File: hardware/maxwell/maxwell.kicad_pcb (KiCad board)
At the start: 2 copper layers, 122 x 59 mm, 91 parts, among them J1 Canbus 1, J10 SPI2_B, J11 BACKUP, J12 UART4, J13 UART5, J14 I2C1, J16 ESP_BM, J17 ESP_PROG, J19 Interconnect (Power), J2 SPI2_C, J20 Interconnect (uC), J3 Neopixel, J4 BOOT0, J5 SPI2_A, J6 Programmer, J7 Dynamo Input, J8 BOOT1, J9 Battery, Q1 BSS138, Q2 PSMN5R4-25YLD, Q3 DMN2400UV, Q4 NTR1P02T1, Q5 NTR1P02T1, U1 MCP1501, U10 MIC39102, U11 AP9101C, U2 SN65HVD233, U3 TPS2113, U4 PCA9536D, U5 ESP-32S, U6 AD7991, U7 STM32F103RETx, U8 TLP188, U9 Buck Regulator, Y1 32.768k, Y2 8M

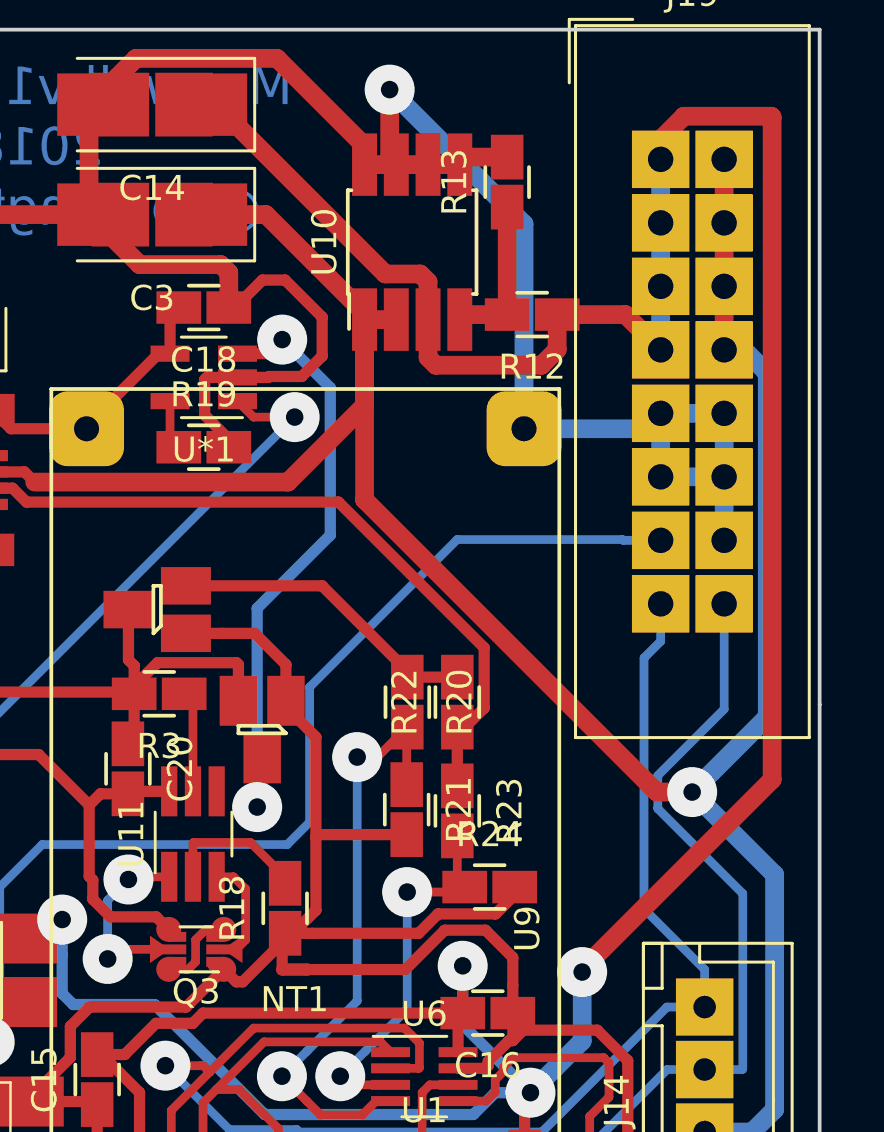
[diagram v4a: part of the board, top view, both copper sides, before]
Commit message: Better SOT-563-LargePads; connect all IDC connector pins on both layers.
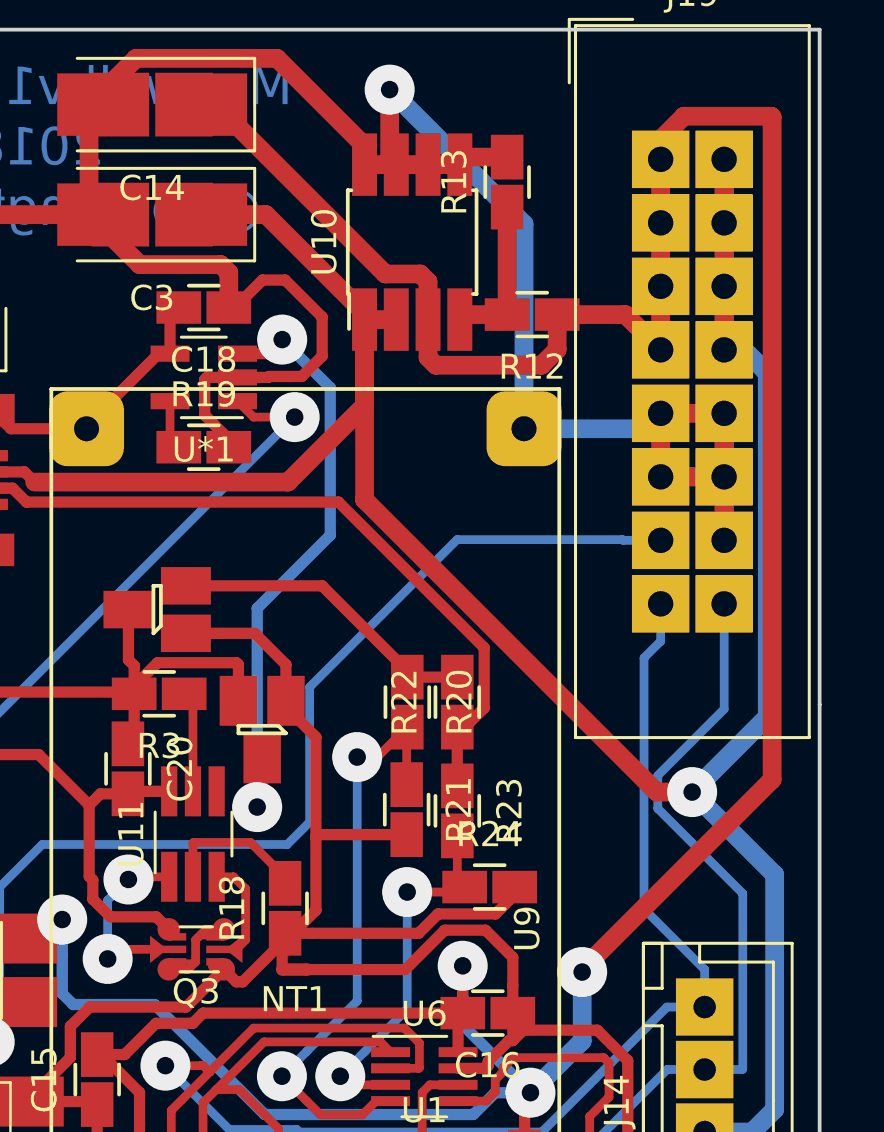
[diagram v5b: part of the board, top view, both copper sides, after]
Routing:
- net GND: track 723.9 -> 736.6 mm
- net VCC: track 292.5 -> 300.1 mm
- net +3V3: track 450.1 -> 457.7 mm
- net Net-(Q3-Pad3): track 3.70 -> 6.03 mm
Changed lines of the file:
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@@
     (thickness 1.6)
     (drawings 16)
-    (tracks 1181)
+    (tracks 1202)
     (zones 0)
     (modules 91)
@@
       (effects (font (size 1 1) (thickness 0.15)))
     )
+    (fp_line (start 1.35 1.1) (end -1.35 1.1) (layer F.CrtYd) (width 0.05))
+    (fp_line (start 1.35 1.1) (end 1.35 -1.1) (layer F.CrtYd) (width 0.05))
+    (fp_line (start -1.35 -1.1) (end -1.35 1.1) (layer F.CrtYd) (width 0.05))
+    (fp_line (start -1.35 -1.1) (end 1.35 -1.1) (layer F.CrtYd) (width 0.05))
+    (fp_line (start 0.65 -0.85) (end -0.3 -0.85) (layer F.Fab) (width 0.1))
+    (fp_line (start 0.65 0.85) (end 0.65 -0.85) (layer F.Fab) (width 0.1))
+    (fp_line (start -0.65 0.85) (end 0.65 0.85) (layer F.Fab) (width 0.1))
+    (fp_line (start -0.65 -0.5) (end -0.65 0.85) (layer F.Fab) (width 0.1))
+    (fp_line (start -0.9 -0.9) (end 0.65 -0.9) (layer F.SilkS) (width 0.12))
+    (fp_line (start 0.65 0.9) (end -0.65 0.9) (layer F.SilkS) (width 0.12))
+    (fp_line (start -0.65 -0.5) (end -0.3 -0.85) (layer F.Fab) (width 0.1))
     (fp_text user %R (at 0 0 270) (layer F.Fab)
       (effects (font (size 0.4 0.4) (thickness 0.0625)))
     )
-    (fp_line (start -0.65 -0.5) (end -0.3 -0.85) (layer F.Fab) (width 0.1))
-    (fp_line (start 0.65 0.9) (end -0.65 0.9) (layer F.SilkS) (width 0.12))
-    (fp_line (start -0.9 -0.9) (end 0.65 -0.9) (layer F.SilkS) (width 0.12))
-    (fp_line (start -0.65 -0.5) (end -0.65 0.85) (layer F.Fab) (width 0.1))
-    (fp_line (start -0.65 0.85) (end 0.65 0.85) (layer F.Fab) (width 0.1))
-    (fp_line (start 0.65 0.85) (end 0.65 -0.85) (layer F.Fab) (width 0.1))
-    (fp_line (start 0.65 -0.85) (end -0.3 -0.85) (layer F.Fab) (width 0.1))
-    (fp_line (start -1.35 -1.1) (end 1.35 -1.1) (layer F.CrtYd) (width 0.05))
-    (fp_line (start -1.35 -1.1) (end -1.35 1.1) (layer F.CrtYd) (width 0.05))
-    (fp_line (start 1.35 1.1) (end 1.35 -1.1) (layer F.CrtYd) (width 0.05))
-    (fp_line (start 1.35 1.1) (end -1.35 1.1) (layer F.CrtYd) (width 0.05))
-    (pad 2 smd trapezoid (at -1.6 0 180) (size 0.5 0.75) (rect_delta 0.35 0 ) (layers F.Cu F.Paste F.Mask)
-      (net 116 "Net-(Q3-Pad2)"))
-    (pad 5 smd trapezoid (at 1.6 0) (size 0.5 0.75) (rect_delta 0.35 0 ) (layers F.Cu F.Paste F.Mask)
+    (pad 5 smd rect (at 0.9 0 180) (size 1 0.3) (layers F.Cu F.Paste F.Mask)
       (net 115 "Net-(Q3-Pad5)"))
-    (pad 3 smd circle (at -1.1 0.8 180) (size 1 1) (layers F.Cu F.Paste F.Mask)
-      (net 117 "Net-(Q3-Pad3)"))
-    (pad 4 smd circle (at 1.1 0.8 180) (size 1 1) (layers F.Cu F.Paste F.Mask)
+    (pad 4 smd rect (at 0.75 0.5 180) (size 0.7 0.3) (layers F.Cu F.Paste F.Mask)
       (net 121 /Power/BATT_PRE_PROT))
-    (pad 6 smd circle (at 1.1 -0.8 180) (size 1 1) (layers F.Cu F.Paste F.Mask)
+    (pad 2 smd rect (at -0.9 0 180) (size 1 0.3) (layers F.Cu F.Paste F.Mask)
+      (net 116 "Net-(Q3-Pad2)"))
+    (pad 6 smd rect (at 0.75 -0.5 180) (size 0.7 0.3) (layers F.Cu F.Paste F.Mask)
       (net 117 "Net-(Q3-Pad3)"))
-    (pad 1 smd circle (at -1.1 -0.8 180) (size 1 1) (layers F.Cu F.Paste F.Mask)
+    (pad 3 smd rect (at -0.75 0.5 180) (size 0.7 0.3) (layers F.Cu F.Paste F.Mask)
+      (net 117 "Net-(Q3-Pad3)"))
+    (pad 1 smd rect (at -0.75 -0.5 180) (size 0.7 0.3) (layers F.Cu F.Paste F.Mask)
       (net 2 GND))
-    (pad 1 smd rect (at -0.75 -0.5 180) (size 0.7 0.4) (layers F.Cu F.Paste F.Mask)
+    (pad 1 smd circle (at -1.1 -0.8 180) (size 0.9 0.9) (layers F.Cu F.Paste F.Mask)
       (net 2 GND))
-    (pad 3 smd rect (at -0.75 0.5 180) (size 0.7 0.4) (layers F.Cu F.Paste F.Mask)
-      (net 117 "Net-(Q3-Pad3)"))
-    (pad 6 smd rect (at 0.75 -0.5 180) (size 0.7 0.4) (layers F.Cu F.Paste F.Mask)
+    (pad 6 smd circle (at 1.1 -0.8 180) (size 0.9 0.9) (layers F.Cu F.Paste F.Mask)
       (net 117 "Net-(Q3-Pad3)"))
-    (pad 2 smd rect (at -0.9 0 180) (size 1 0.4) (layers F.Cu F.Paste F.Mask)
-      (net 116 "Net-(Q3-Pad2)"))
-    (pad 4 smd rect (at 0.75 0.5 180) (size 0.7 0.4) (layers F.Cu F.Paste F.Mask)
+    (pad 4 smd circle (at 1.1 0.8 180) (size 0.9 0.9) (layers F.Cu F.Paste F.Mask)
       (net 121 /Power/BATT_PRE_PROT))
-    (pad 5 smd rect (at 0.9 0 180) (size 1 0.4) (layers F.Cu F.Paste F.Mask)
+    (pad 3 smd circle (at -1.1 0.8 180) (size 0.9 0.9) (layers F.Cu F.Paste F.Mask)
+      (net 117 "Net-(Q3-Pad3)"))
+    (pad 5 smd trapezoid (at 1.6 0) (size 0.5 0.7) (rect_delta 0.4 0 ) (layers F.Cu F.Paste F.Mask)
       (net 115 "Net-(Q3-Pad5)"))
+    (pad 2 smd trapezoid (at -1.6 0 180) (size 0.5 0.7) (rect_delta 0.4 0 ) (layers F.Cu F.Paste F.Mask)
+      (net 116 "Net-(Q3-Pad2)"))
     (model ${KISYS3DMOD}/Package_TO_SOT_SMD.3dshapes/SOT-563.wrl
       (at (xyz 0 0 0))
@@
   (segment (start 89.5 113.458991) (end 87.433438 115.525553) (width 0.75) (layer B.Cu) (net 1))
   (segment (start 89.5 110.7) (end 89.5 113.458991) (width 0.75) (layer B.Cu) (net 1))
+  (segment (start 92.64 78.19) (end 92.64 80.73) (width 0.75) (layer F.Cu) (net 1))
+  (segment (start 92.64 80.73) (end 92.64 83.27) (width 0.75) (layer F.Cu) (net 1))
+  (segment (start 92.64 83.27) (end 92.64 85.81) (width 0.75) (layer F.Cu) (net 1))
   (segment (start 121.527 97.947) (end 121.527 100.617) (width 0.45) (layer F.Cu) (net 2) (status 20))
   (segment (start 122.320082 98.740082) (end 121.527 97.947) (width 0.45) (layer F.Cu) (net 2))
@@
   (segment (start 81.8 78.135) (end 82.065 78.4) (width 0.75) (layer F.Cu) (net 2))
   (segment (start 81.8 75.4) (end 81.8 78.135) (width 0.75) (layer F.Cu) (net 2))
+  (segment (start 92.64 88.35) (end 95.18 88.35) (width 0.75) (layer F.Cu) (net 2))
+  (segment (start 95.18 88.35) (end 95.18 90.89) (width 0.75) (layer F.Cu) (net 2))
+  (segment (start 95.18 90.89) (end 92.64 90.89) (width 0.75) (layer F.Cu) (net 2))
+  (segment (start 92.64 88.35) (end 92.64 90.89) (width 0.75) (layer F.Cu) (net 2))
+  (segment (start 95.18 90.89) (end 95.18 93.43) (width 0.75) (layer F.Cu) (net 2))
   (segment (start 63.888 92.712) (end 63.888 93.812) (width 0.45) (layer F.Cu) (net 3))
   (segment (start 63.888 92.086) (end 63.888 92.712) (width 0.45) (layer F.Cu) (net 3))
@@
   (segment (start 97.2 116.2) (end 96.3 117.1) (width 0.75) (layer B.Cu) (net 47))
   (segment (start 97.2 106.8) (end 97.2 116.2) (width 0.75) (layer B.Cu) (net 47))
+  (segment (start 95.18 78.19) (end 95.18 80.73) (width 0.75) (layer B.Cu) (net 47))
+  (segment (start 95.18 80.73) (end 95.18 83.27) (width 0.75) (layer B.Cu) (net 47))
+  (segment (start 95.18 83.27) (end 95.18 85.81) (width 0.75) (layer B.Cu) (net 47))
   (segment (start 115.31 83.86) (end 114.93 83.48) (width 0.35) (layer F.Cu) (net 48) (status 30))
   (segment (start 116.635 83.86) (end 115.31 83.86) (width 0.35) (layer F.Cu) (net 48) (status 30))
@@
   (segment (start 75.662 109.792) (end 76.037001 109.416999) (width 0.35) (layer F.Cu) (net 116))
   (segment (start 73.669106 110.592) (end 72.962 110.592) (width 0.35) (layer F.Cu) (net 117))
-  (segment (start 74.037001 110.292001) (end 73.737002 110.592) (width 0.35) (layer F.Cu) (net 117))
   (segment (start 73.737002 110.592) (end 73.669106 110.592) (width 0.35) (layer F.Cu) (net 117))
-  (segment (start 74.454894 108.992) (end 74.037001 109.409893) (width 0.35) (layer F.Cu) (net 117))
   (segment (start 74.037001 109.409893) (end 74.037001 110.292001) (width 0.35) (layer F.Cu) (net 117))
   (segment (start 75.162 108.992) (end 74.454894 108.992) (width 0.35) (layer F.Cu) (net 117))
+  (segment (start 75.112 108.992) (end 74.812 109.292) (width 0.2) (layer F.Cu) (net 117))
+  (segment (start 75.162 108.992) (end 75.112 108.992) (width 0.2) (layer F.Cu) (net 117))
+  (segment (start 74.812 109.292) (end 74.154894 109.292) (width 0.2) (layer F.Cu) (net 117))
+  (segment (start 74.154894 109.292) (end 74.146894 109.3) (width 0.2) (layer F.Cu) (net 117))
+  (segment (start 74.454894 108.992) (end 74.146894 109.3) (width 0.35) (layer F.Cu) (net 117))
+  (segment (start 74.146894 109.3) (end 74.037001 109.409893) (width 0.35) (layer F.Cu) (net 117))
+  (segment (start 73.012 110.592) (end 73.312 110.292) (width 0.2) (layer F.Cu) (net 117))
+  (segment (start 72.962 110.592) (end 73.012 110.592) (width 0.2) (layer F.Cu) (net 117))
+  (segment (start 74.021002 110.292) (end 74.029002 110.3) (width 0.2) (layer F.Cu) (net 117))
+  (segment (start 73.312 110.292) (end 74.021002 110.292) (width 0.2) (layer F.Cu) (net 117))
+  (segment (start 74.037001 110.292001) (end 74.029002 110.3) (width 0.35) (layer F.Cu) (net 117))
+  (segment (start 74.029002 110.3) (end 73.737002 110.592) (width 0.35) (layer F.Cu) (net 117))
   (segment (start 81.476 120.417) (end 81.476 119.642) (width 0.45) (layer F.Cu) (net 120))
   (segment (start 81.476 120.976) (end 81.476 120.417) (width 0.45) (layer F.Cu) (net 120))

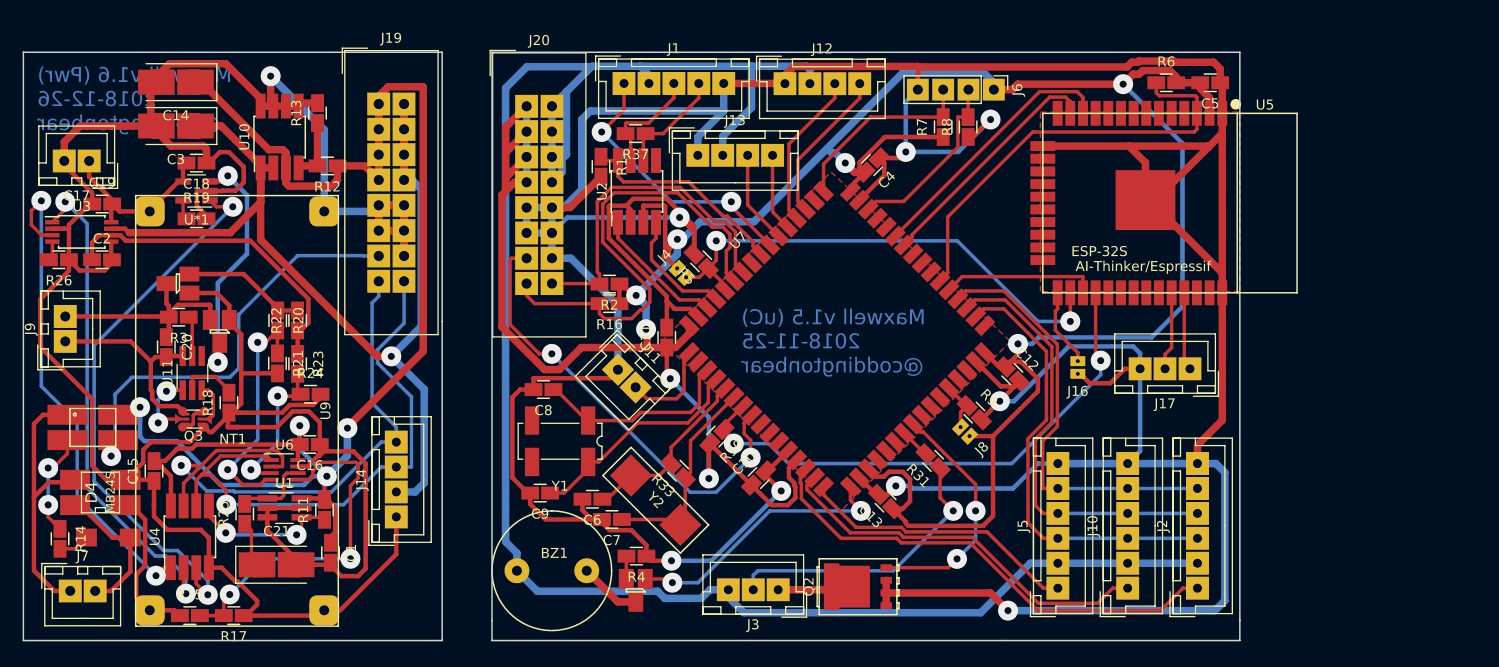
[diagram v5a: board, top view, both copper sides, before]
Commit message: Updating PWR board to v1.7; adds:
* Fix for footprint of AP9101C (I have the five-pin package; not six)
* Grounding VM on the AP9101C to BAT- to disable current protection;
  I'm using the TPS2113A for current protection, so this feature isn't
  needed.
* Adds I2C-addressable INA219AID current sensor IC.
* Adds I2C-addressable PCF8593 counter for speed measurement.
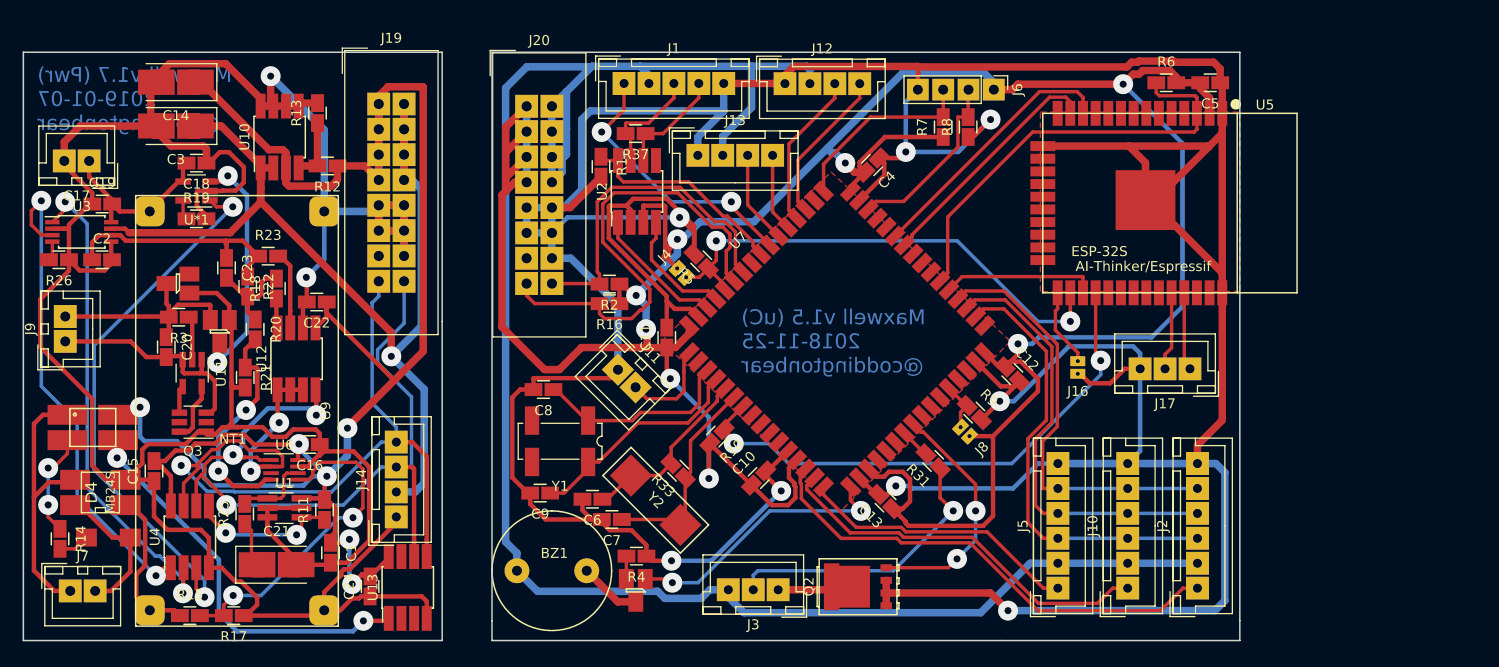
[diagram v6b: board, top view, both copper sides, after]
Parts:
- removed R24: ANY, coddingtonbear:0805_Milling
- added C22: 0.1u, coddingtonbear:0805_Milling, F.Cu at (86.4, 98.0)
- added C23: 0.1u, coddingtonbear:0805_Milling, F.Cu at (77.4, 94.6)
- added C24: 0.1u, coddingtonbear:0805_Milling, F.Cu at (91.8, 126.6)
- added U12: INA219AID, coddingtonbear:SOIC-8_3.9x4.9mm_P1.27mm_LargePads, F.Cu at (84.4, 103.8)
- added U13: PCF8593, coddingtonbear:SOIC-8_3.9x4.9mm_P1.27mm_LargePads, F.Cu at (95.5, 126.7)
- Q3: value DMN2400UV -> DMG9926UDM; footprint coddingtonbear:SOT-563-LargePads -> Package_TO_SOT_SMD:SOT-23-6_Handsoldering
- R18: value 2.7k -> 10
- R23: value ANY -> 10
- U11: value AP9101C -> AP9101C-SOT-25; footprint Package_TO_SOT_SMD:TSOT-23-6_HandSoldering -> Package_TO_SOT_SMD:SOT-23-5_HandSoldering
- moved R18 12.4 mm to (82.4, 96.7)
- moved R23 11.2 mm to (81.5, 93.5), turned to 0 degrees
- moved R22 6.05 mm to (79.5, 96.5), turned to 270 degrees
- moved R21 3.53 mm to (79.2, 105.6)
- moved R20 2.43 mm to (80.2, 100.8)
- moved Q3 0.31 mm to (74.0, 110.1)
- turned U11 to 270 degrees
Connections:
- J19 pad 13: SPEED -> Net-(J19-Pad13)
- J20 pad 13: SPEED -> Net-(J20-Pad13)
- Q3 pad 3: Net-(Q3-Pad3) -> /Power/BATT_PRE_PROT
- Q3 pad 4: /Power/BATT_PRE_PROT -> Net-(Q3-Pad4)
- Q3 pad 6: Net-(Q3-Pad3) -> Net-(Q3-Pad6)
- Q5 pad 2: /Power/BATT_PRE_SENSE -> Net-(Q5-Pad2)
- R18 pad 1: GND -> Net-(R18-Pad1)
- R18 pad 2: Net-(R18-Pad2) -> Net-(C23-Pad2)
- R20 pad 1: /Power/BATT_PRE_SENSE -> Net-(C23-Pad2)
- R22 pad 2: /Power/BATT_PRE_SENSE -> Net-(C23-Pad2)
- R23 pad 2: CURRENT_SENSE -> Net-(R23-Pad2)
- U11 pad 1: Net-(Q3-Pad5) -> /Power/BATT_PRE_PROT
- U11 pad 2: Net-(R18-Pad2) -> Net-(R3-Pad1)
- U11 pad 3: Net-(Q3-Pad2) -> /Power/BATT_PRE_PROT
- U11 pad 4: (no net) -> Net-(Q3-Pad4)
- U11 pad 5: Net-(R3-Pad1) -> Net-(Q3-Pad6)
- U6 pad 3: CURRENT_SENSE -> Net-(U6-Pad3)
- U7 pad 8: SPEED -> Net-(U7-Pad8)
- U8 pad 4: SPEED -> Net-(U13-Pad1)
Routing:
- net SPEED: track 89.2 -> 0.00 mm, vias 3 -> 0
- net Net-(U13-Pad1): track 0.00 -> 40.0 mm, vias 0 -> 2
- net I2C1_SDA: track 107.6 -> 136.6 mm, vias 1 -> 3
- net I2C1_SCL: track 90.8 -> 116.5 mm, vias 1 -> 3
- net +3V3: track 457.7 -> 480.8 mm, vias 12 -> 14
- net CURRENT_SENSE: track 15.2 -> 0.00 mm, vias 2 -> 0
- net /Power/BATT_PRE_SENSE: track 12.5 -> 0.00 mm
- net Net-(C23-Pad2): track 0.00 -> 9.79 mm
- net GND: track 736.6 -> 745.9 mm, vias 9 -> 10
- net +BATT: track 32.5 -> 23.8 mm
- net Net-(Q3-Pad5): track 7.99 -> 0.00 mm, vias 2 -> 0
- net Net-(R23-Pad2): track 0.00 -> 7.85 mm
- net Net-(Q3-Pad3): track 6.03 -> 0.00 mm
- net Net-(Q3-Pad6): track 0.00 -> 5.98 mm
- net Net-(R18-Pad2): track 5.87 -> 0.00 mm
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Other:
- net class Default: trace_width 0.35 -> 0.45
- board text added: "Maxwell v1.7 (Pwr) 2019-01-07 @coddingtonbear"
- board text removed: "Maxwell v1.6 (Pwr) 2018-12-26 @coddingtonbear"

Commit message: Final modifications for Rev 1.7.
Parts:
- added R24: 10k, coddingtonbear:0805_Milling, F.Cu at (58.8, 84.3)
- moved C17 5.63 mm to (63.5, 78.3)
- moved NT1 2.82 mm to (80.8, 110.9), turned to 90 degrees
- moved C20 2.62 mm to (69.5, 100.8)
- moved U11 2.54 mm to (72.0, 103.5)
- moved Q3 1.99 mm to (72.9, 108.4)
- moved C24 1.26 mm to (90.5, 126.3)
- moved U13 1.26 mm to (94.3, 126.4)
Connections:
- net /Power/BATT_PRE_POLARITY renamed /Power/BATT+
- net /Power/BATT_PRE_PROT renamed /Power/BATT-UNPROT
- Q5 pad 2: Net-(Q5-Pad2) -> Net-(C23-Pad2)
- U13 pad 3: Net-(U13-Pad3) -> +3V3
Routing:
- net +3V3: track 480.8 -> 502.1 mm
- net I2C1_SDA: track 136.6 -> 151.5 mm
- net GND: track 745.9 -> 756.9 mm
- net /Power/+Dynamo_Buck: track 17.9 -> 23.5 mm
- net Net-(C23-Pad2): track 9.79 -> 13.7 mm
- net /Power/BATT-UNPROT: track 22.4 -> 19.7 mm
- net DISABLE_BATTERY_SRC: track 49.5 -> 52.2 mm
- net DYNAMO_VOLTAGE: track 33.2 -> 30.8 mm
- net /Power/BATT+: track 22.3 -> 20.4 mm
- net Net-(U13-Pad1): track 40.0 -> 38.9 mm
- net I2C1_SCL: track 116.5 -> 117.3 mm
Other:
- board text added: "+"
